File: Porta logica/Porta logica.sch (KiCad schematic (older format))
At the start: 56 parts, among them P1 Input, P2 Out, SW1 SW_PUSH, SW2 SW_PUSH, U1 74HC595, U2 74HC595, U3 74HC00, U4 74HC595

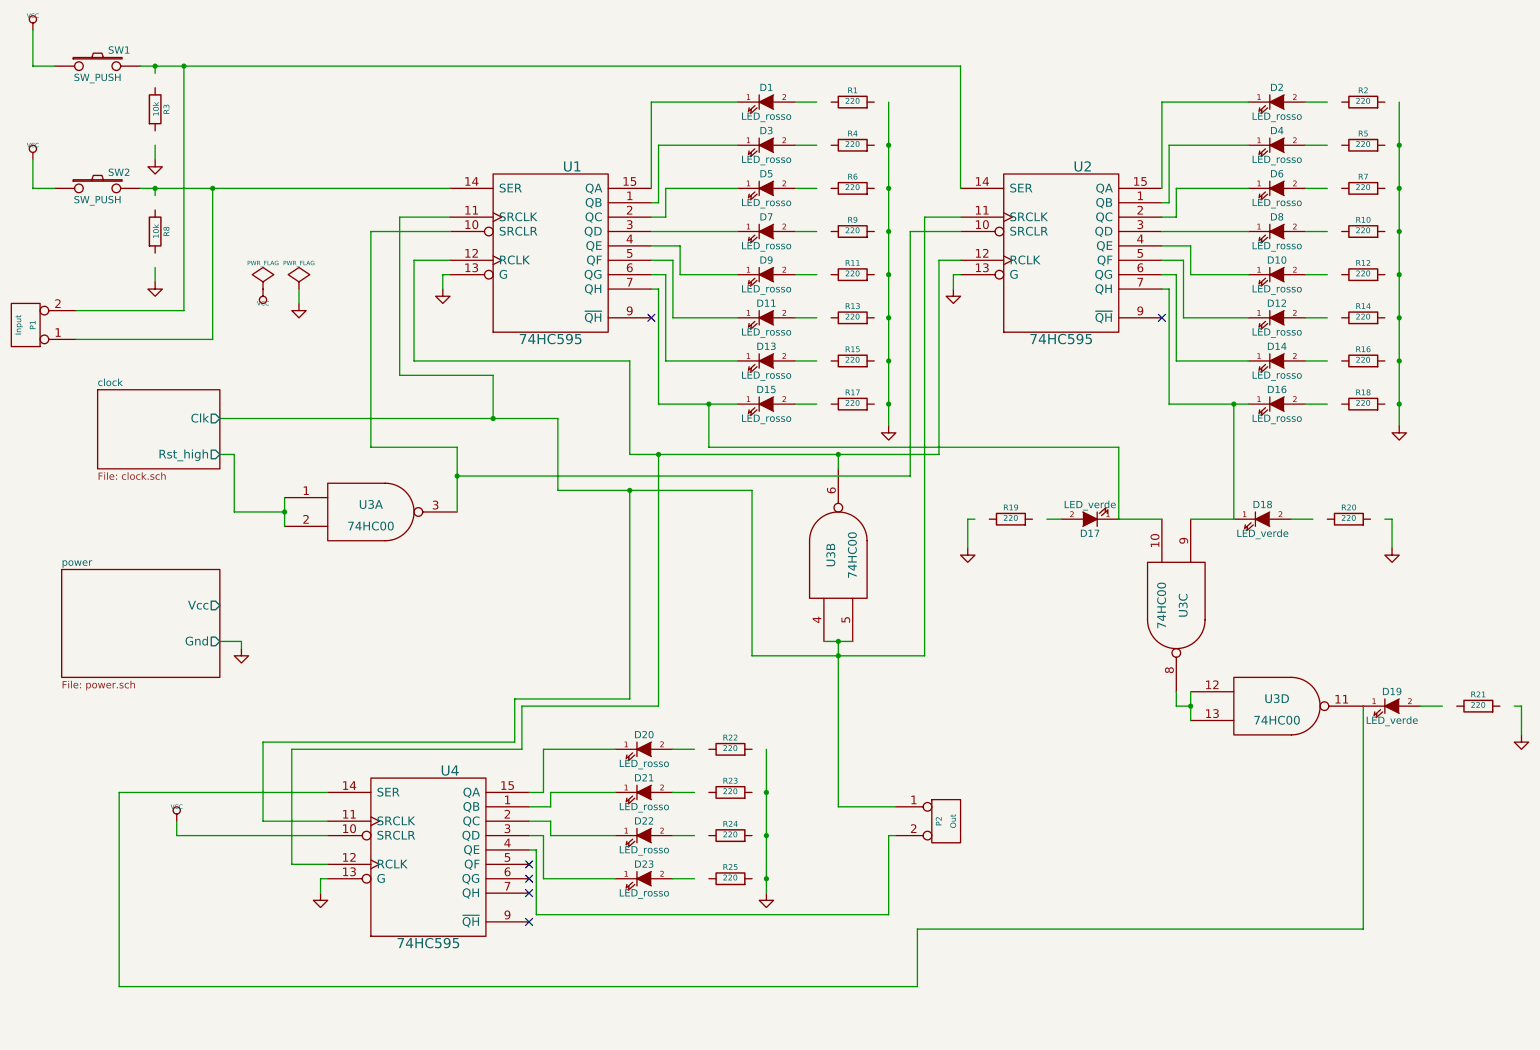
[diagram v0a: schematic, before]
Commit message: correzione bug, migliorie grafiche
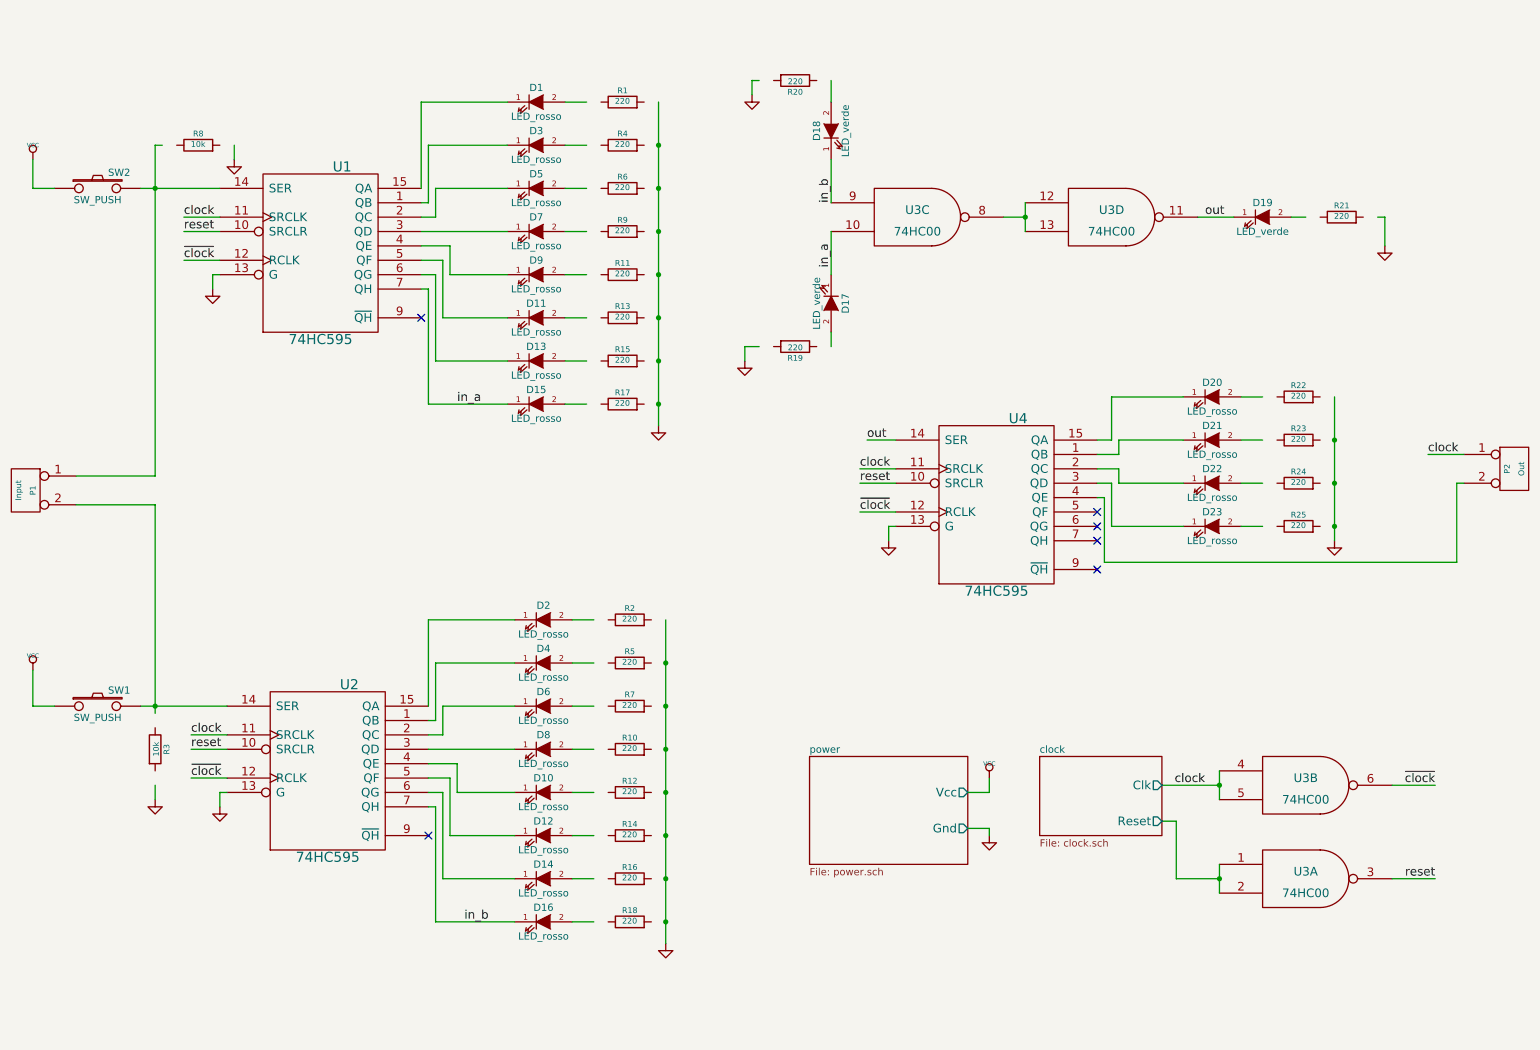
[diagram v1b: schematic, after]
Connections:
- net labels added: clock, in_a, in_b, out, reset, ~clock
- wire segments 177 -> 138
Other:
- moved on the sheet: D1, D10, D11, D12, D13, D14, D15, D16, D17, D18, D19, D2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

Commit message: Riordinato tutto lo schematico, eliminato power
Il contenuto di power.sch sta nello schematico principale. Fixato anche
il latch "fatto in casa", è default basso, non alto!
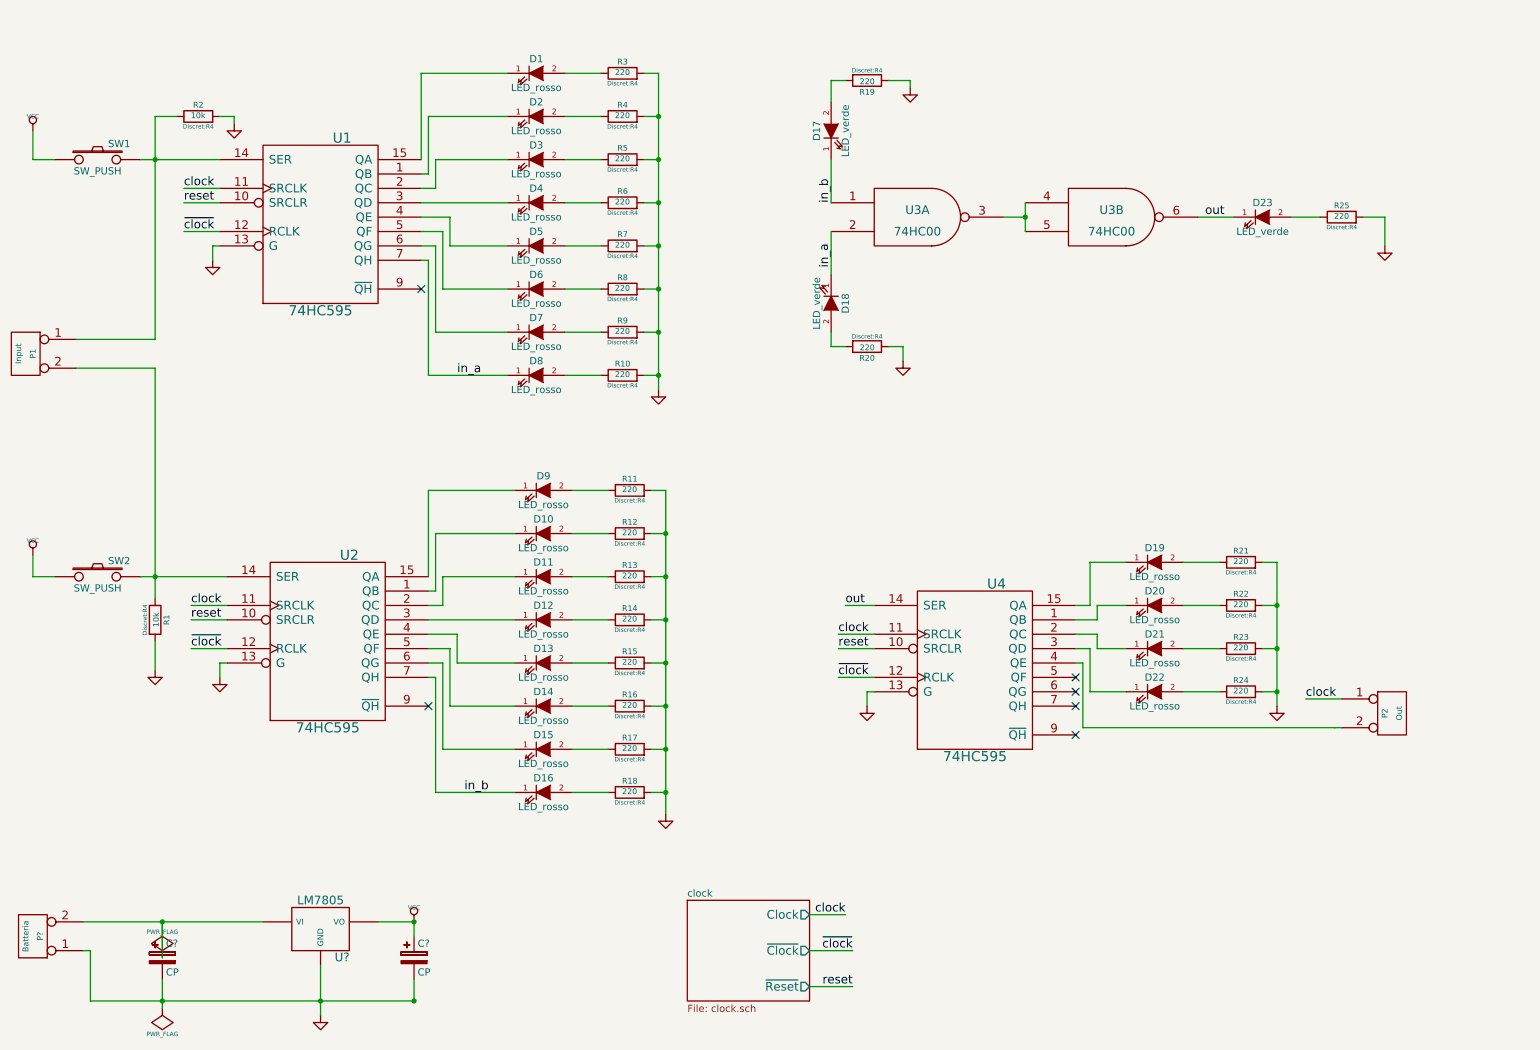
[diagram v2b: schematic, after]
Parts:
- removed unit 2 of U3
- removed unit 1 of U3
- added C? (x2): CP, symbol CP
- added P?: Batteria, Pin_Headers:Pin_Header_Straight_1x02, symbol CONN_2
- added U?: LM7805, Power_Integrations:TO-220, symbol LM7805
- D1, D16: footprint ~ -> LEDs:LED-5MM
- D10: renamed from D4; footprint ~ -> LEDs:LED-5MM
- D11: renamed from D6; footprint ~ -> LEDs:LED-5MM
- D12: renamed from D8; footprint ~ -> LEDs:LED-5MM
- D13: renamed from D10; footprint ~ -> LEDs:LED-5MM
- D14: renamed from D12; footprint ~ -> LEDs:LED-5MM
- D15: renamed from D14; footprint ~ -> LEDs:LED-5MM
- D17: renamed from D18; footprint ~ -> LEDs:LED-5MM
- D18: renamed from D17; footprint ~ -> LEDs:LED-5MM
- D19: renamed from D20; footprint ~ -> LEDs:LED-5MM
- D2: renamed from D3; footprint ~ -> LEDs:LED-5MM
- D20: renamed from D21; footprint ~ -> LEDs:LED-5MM
- D21: renamed from D22; footprint ~ -> LEDs:LED-5MM
- D22: renamed from D23; footprint ~ -> LEDs:LED-5MM
- D23: renamed from D19; footprint ~ -> LEDs:LED-5MM
- D3: renamed from D5; footprint ~ -> LEDs:LED-5MM
- D4: renamed from D7; footprint ~ -> LEDs:LED-5MM
- D5: renamed from D9; footprint ~ -> LEDs:LED-5MM
- D6: renamed from D11; footprint ~ -> LEDs:LED-5MM
- D7: renamed from D13; footprint ~ -> LEDs:LED-5MM
- D8: renamed from D15; footprint ~ -> LEDs:LED-5MM
- D9: renamed from D2; footprint ~ -> LEDs:LED-5MM
- P1, P2: footprint (none) -> Pin_Headers:Pin_Header_Straight_1x02
- R1: renamed from R3; footprint ~ -> Discret:R4
- R10: renamed from R17; footprint ~ -> Discret:R4
- R11: renamed from R2; footprint ~ -> Discret:R4
- R12: renamed from R5; footprint ~ -> Discret:R4
- R13: renamed from R7; footprint ~ -> Discret:R4
- R14: renamed from R10; footprint ~ -> Discret:R4
- R15: renamed from R12; footprint ~ -> Discret:R4
- R16: renamed from R14; footprint ~ -> Discret:R4
- R17: renamed from R16; footprint ~ -> Discret:R4
- R18, R4: footprint ~ -> Discret:R4
- R19: renamed from R20; footprint ~ -> Discret:R4
- R2: renamed from R8; footprint ~ -> Discret:R4
- R20: renamed from R19; footprint ~ -> Discret:R4
- R21: renamed from R22; footprint ~ -> Discret:R4
- R22: renamed from R23; footprint ~ -> Discret:R4
- R23: renamed from R24; footprint ~ -> Discret:R4
- R24: renamed from R25; footprint ~ -> Discret:R4
- R25: renamed from R21; footprint ~ -> Discret:R4
- R3: renamed from R1; footprint ~ -> Discret:R4
- R5: renamed from R6; footprint ~ -> Discret:R4
- R6: renamed from R9; footprint ~ -> Discret:R4
- R7: renamed from R11; footprint ~ -> Discret:R4
- R8: renamed from R13; footprint ~ -> Discret:R4
- R9: renamed from R15; footprint ~ -> Discret:R4
- SW1: renamed from SW2; footprint ~ -> Buttons_Switches_ThroughHole:SW_PUSH_SMALL
- SW2: renamed from SW1; footprint ~ -> Buttons_Switches_ThroughHole:SW_PUSH_SMALL
- U1, U2, U4: footprint ~ -> Housings_SOIC:SOIC-16_7.5x10.3mm_Pitch1.27mm
- U3: footprint ~ -> Housings_SOIC:SOIC-14_3.9x8.7mm_Pitch1.27mm
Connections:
- wire segments 138 -> 190
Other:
- moved on the sheet: D1, D10, D11, D12, D13, D14, D15, D16, D19, D2, D20, D21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

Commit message: Completata annotazione e associazione di footprint
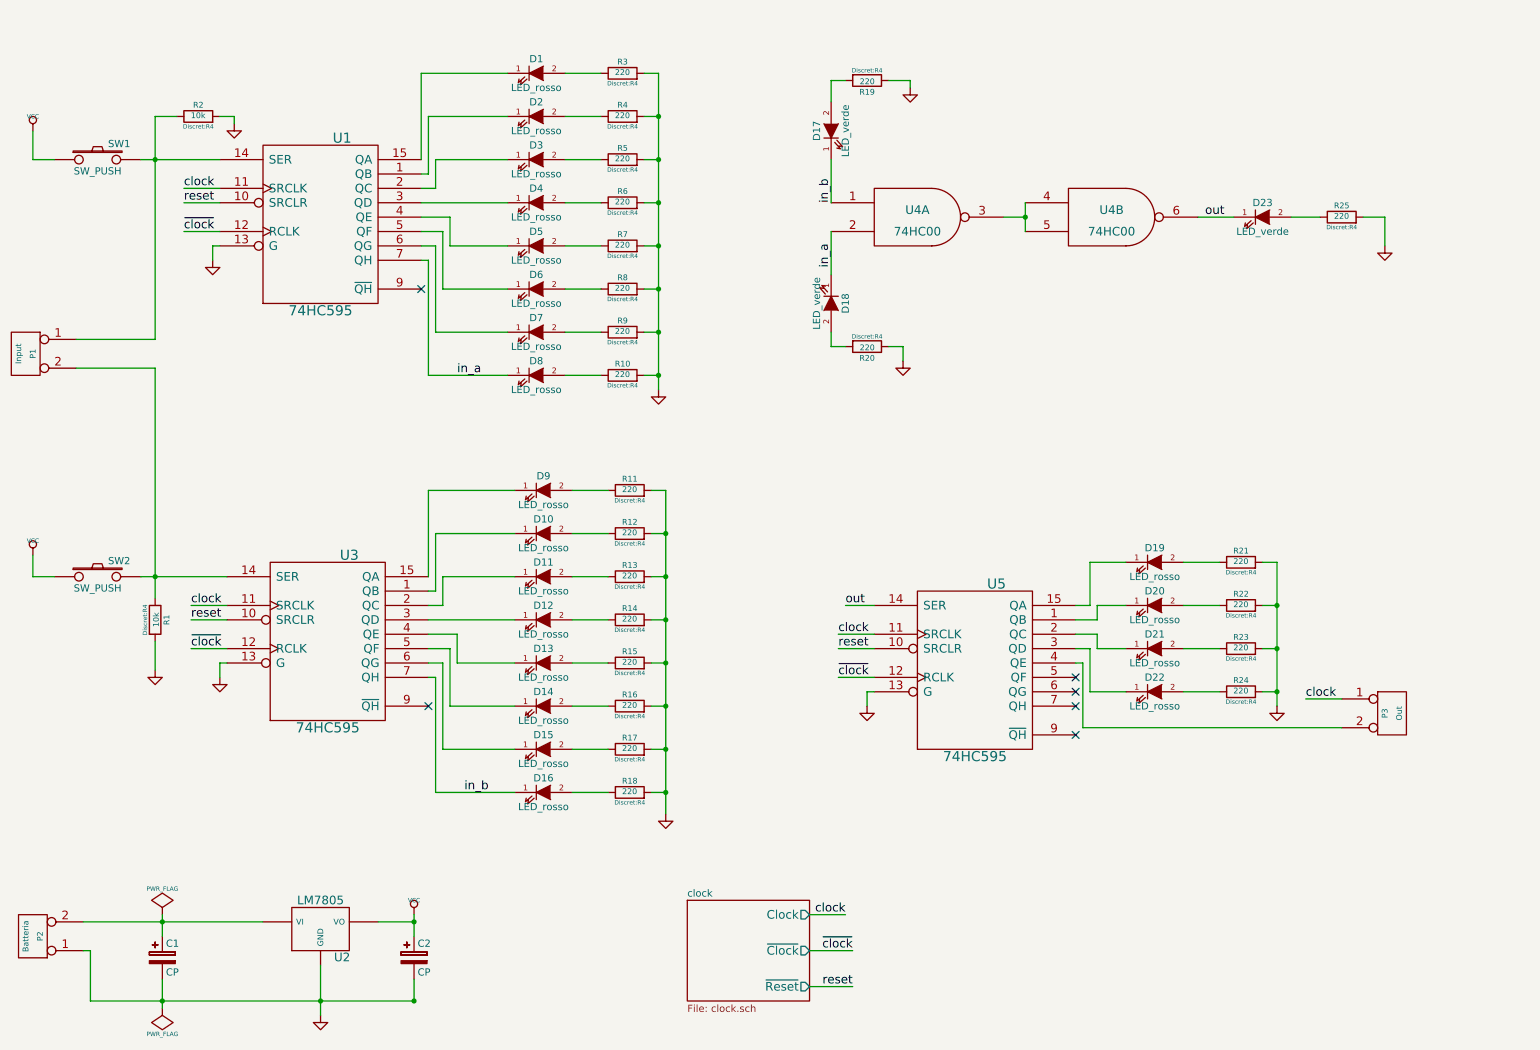
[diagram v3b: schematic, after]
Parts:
- C1, C2: renamed from C?; footprint (none) -> Capacitors_Elko_ThroughHole:Elko_vert_11.2x6.3mm_RM2.5
- U2: renamed from U?; footprint Power_Integrations:TO-220 -> Housings_SOIC:SOIC-16_7.5x10.3mm_Pitch1.27mm
- U3: renamed from U2; footprint Housings_SOIC:SOIC-16_7.5x10.3mm_Pitch1.27mm -> Housings_SOIC:SOIC-14_3.9x8.7mm_Pitch1.27mm
- U4: renamed from U3; footprint Housings_SOIC:SOIC-14_3.9x8.7mm_Pitch1.27mm -> Housings_SOIC:SOIC-16_7.5x10.3mm_Pitch1.27mm
- U5: renamed from U4; footprint Housings_SOIC:SOIC-16_7.5x10.3mm_Pitch1.27mm -> Power_Integrations:TO-220
- gave numbers to parts that had none: 1
- renumbered P2 to P3
